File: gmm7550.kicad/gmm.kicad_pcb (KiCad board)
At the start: 6 copper layers, 50 x 75 mm, 252 parts, among them P1 10144518-061802LF, P2 10144518-061802LF, P3 10144518-061802LF, P4 10144518-061802LF, P5 10144518-061802LF, U1 CCGM1A1, U10 PCA9539AHF, U11 TPS3840DL28DBV, U12 ADP2164, U13 ADP2164, U2 CDCE6214, U3 ADP1753, U4 STG3692, U5 STG3692, U6 74LVC1G08, U7 74LVC1G07, U8 STG3692, U9 IS25LQ032B-JNLE, Y1 NX3225SA

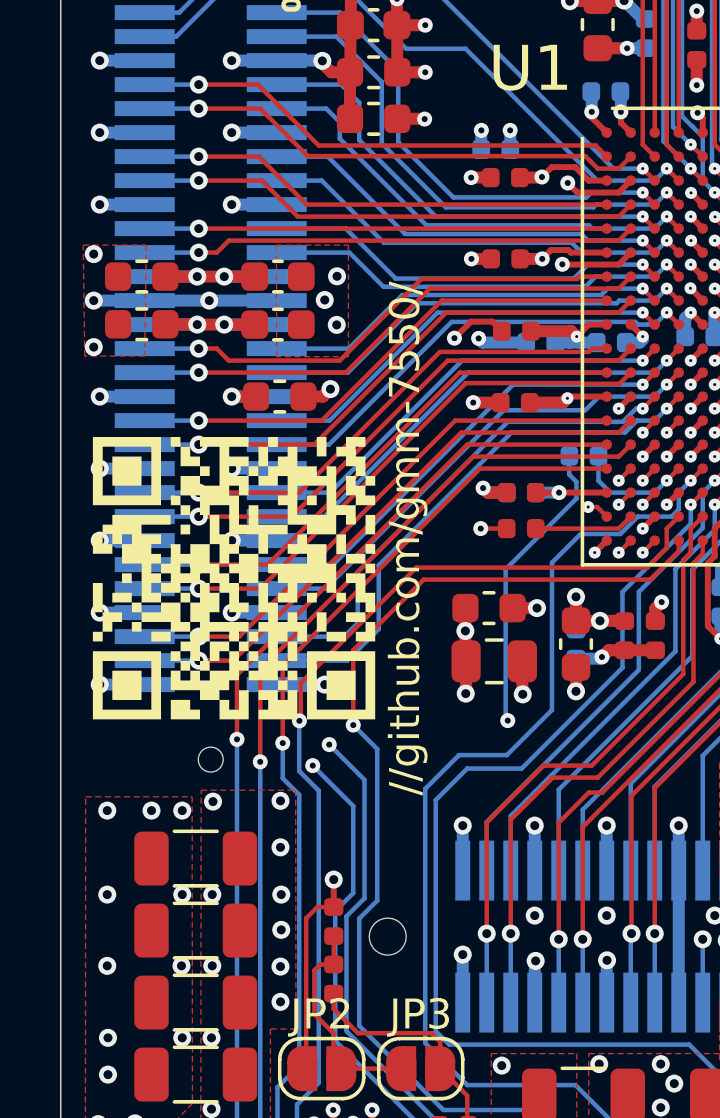
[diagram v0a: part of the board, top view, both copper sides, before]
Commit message: Update QR-code with a link to the project web site
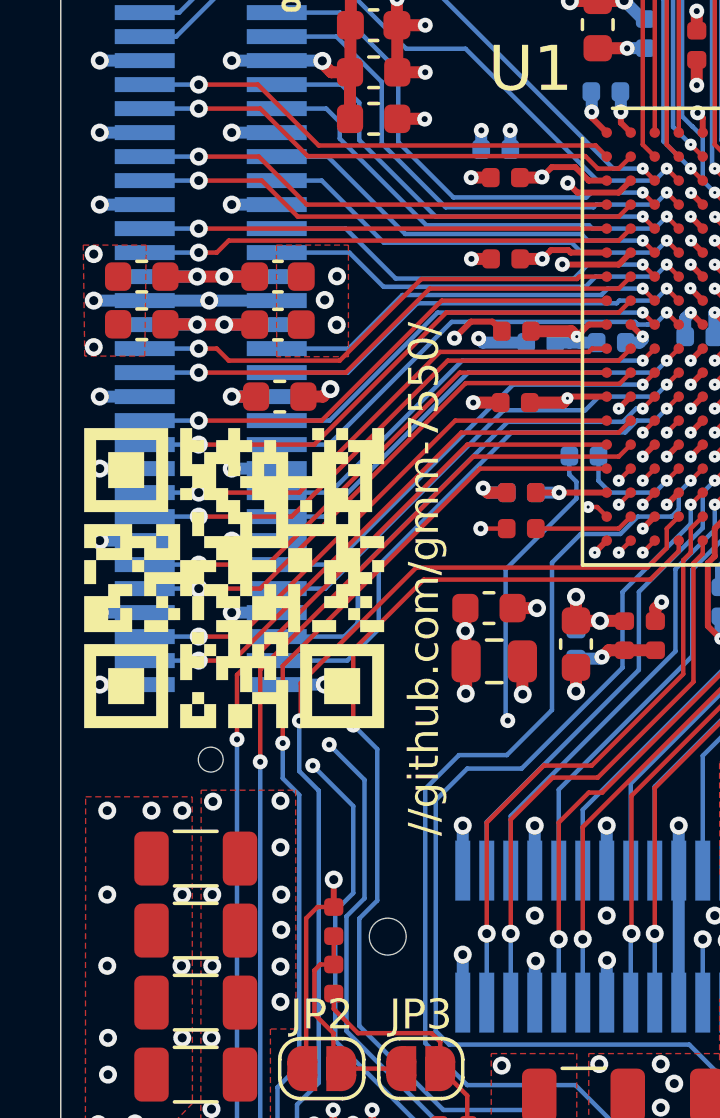
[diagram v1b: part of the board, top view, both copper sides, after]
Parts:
- QR1: footprint gmm:GitHub_link_QR -> gmm:gmm7550_dev_link_QR
